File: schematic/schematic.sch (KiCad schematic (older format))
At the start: 1 part

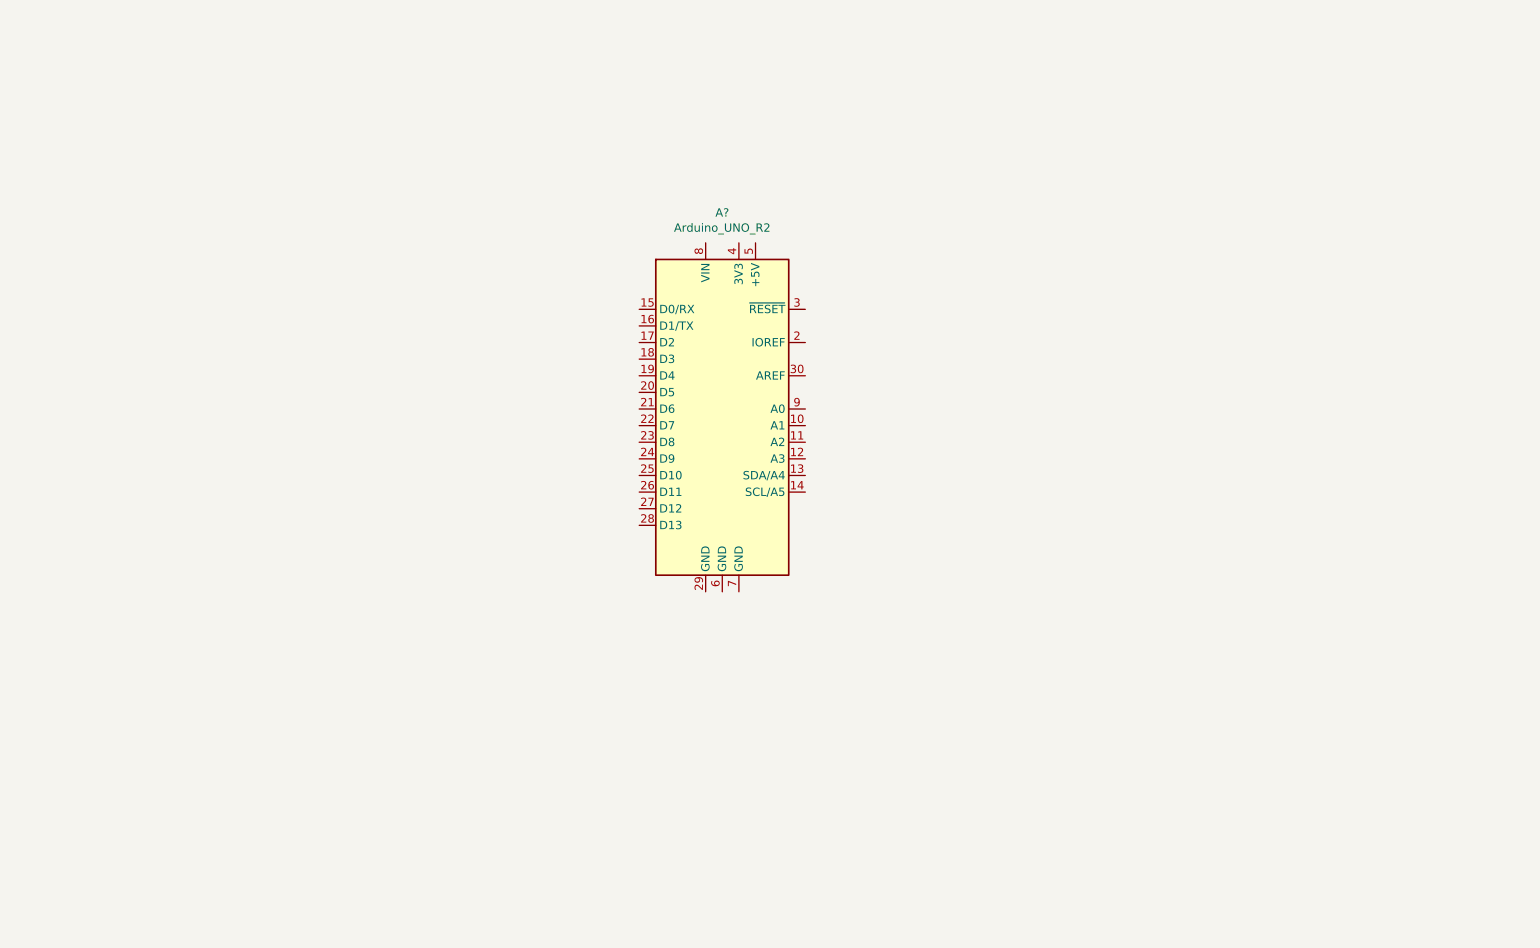
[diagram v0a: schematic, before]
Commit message: Finish pressure sensor symbol, start wiring
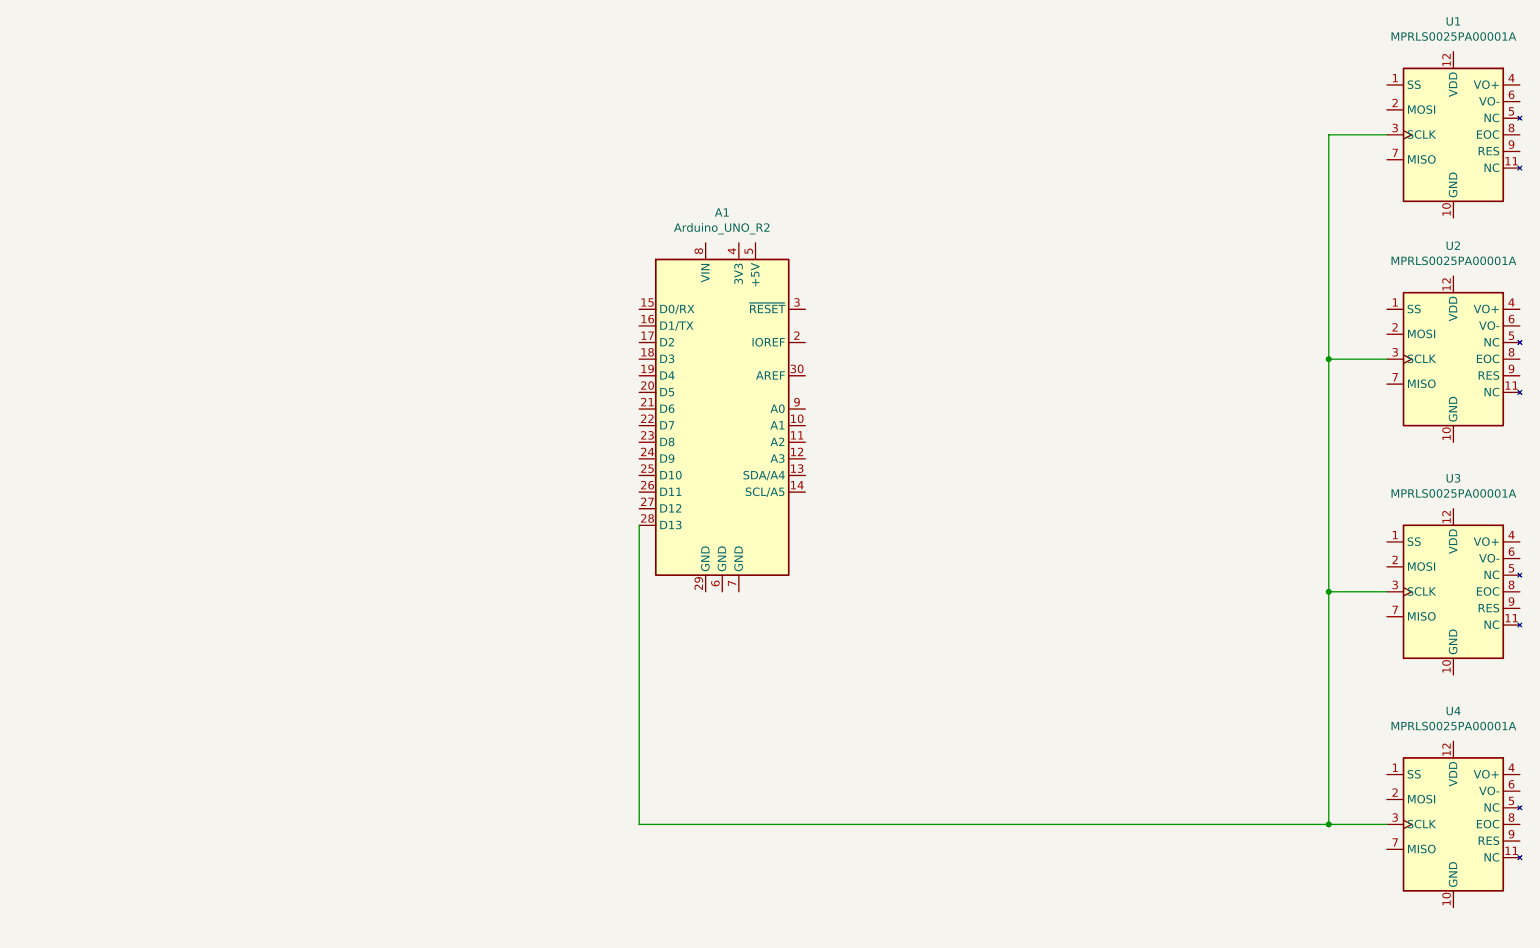
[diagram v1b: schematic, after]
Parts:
- added U1, U2, U3, U4: MPRLS0025PA00001A, symbol ventilator:MPRLS0025PA00001A
- gave numbers to parts that had none: 1
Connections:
- net at A1.28 (D13): now also U1.3 (SCLK), U2.3 (SCLK), U3.3 (SCLK), U4.3 (SCLK)
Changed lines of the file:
@@
 encoding utf-8
 Sheet 1 1
-Title ""
+Title "Ventilator"
 Date ""
-Rev ""
+Rev "1A"
 Comp ""
 Comment1 ""
@@
 $EndDescr
 $Comp
-L MCU_Module:Arduino_UNO_R2 A?
+L MCU_Module:Arduino_UNO_R2 A1
 U 1 1 5E80F89B
 P 5900 3050
-F 0 "A?" H 5900 4231 50  0000 C CNN
+F 0 "A1" H 5900 4231 50  0000 C CNN
 F 1 "Arduino_UNO_R2" H 5900 4140 50  0000 C CNN
 F 2 "Module:Arduino_UNO_R2" H 5900 3050 50  0001 C CIN
@@
 	1    0    0    -1
 $EndComp
+$Comp
+L ventilator:MPRLS0025PA00001A U1
+U 1 1 5E810603
+P 10300 1400
+F 0 "U1" H 10300 2081 50  0000 C CNN
+F 1 "MPRLS0025PA00001A" H 10300 1990 50  0000 C CNN
+F 2 "" H 11300 950 50  0001 C CNN
+F 3 "https://sensing.honeywell.com/index.php?ci_id=172626" H 11450 1450 50  0001 C CNN
+	1    10300 1400
+	1    0    0    -1
+$EndComp
+$Comp
+L ventilator:MPRLS0025PA00001A U2
+U 1 1 5E8111B8
+P 10300 2750
+F 0 "U2" H 10300 3431 50  0000 C CNN
+F 1 "MPRLS0025PA00001A" H 10300 3340 50  0000 C CNN
+F 2 "" H 11300 2300 50  0001 C CNN
+F 3 "https://sensing.honeywell.com/index.php?ci_id=172626" H 11450 2800 50  0001 C CNN
+	1    10300 2750
+	1    0    0    -1
+$EndComp
+$Comp
+L ventilator:MPRLS0025PA00001A U3
+U 1 1 5E811D8D
+P 10300 4150
+F 0 "U3" H 10300 4831 50  0000 C CNN
+F 1 "MPRLS0025PA00001A" H 10300 4740 50  0000 C CNN
+F 2 "" H 11300 3700 50  0001 C CNN
+F 3 "https://sensing.honeywell.com/index.php?ci_id=172626" H 11450 4200 50  0001 C CNN
+	1    10300 4150
+	1    0    0    -1
+$EndComp
+$Comp
+L ventilator:MPRLS0025PA00001A U4
+U 1 1 5E8127FE
+P 10300 5550
+F 0 "U4" H 10300 6231 50  0000 C CNN
+F 1 "MPRLS0025PA00001A" H 10300 6140 50  0000 C CNN
+F 2 "" H 11300 5100 50  0001 C CNN
+F 3 "https://sensing.honeywell.com/index.php?ci_id=172626" H 11450 5600 50  0001 C CNN
+	1    10300 5550
+	1    0    0    -1
+$EndComp
+Wire Wire Line
+	5400 5550 9550 5550
+Wire Wire Line
+	5400 3750 5400 5550
+Wire Wire Line
+	9900 4150 9550 4150
+Wire Wire Line
+	9550 4150 9550 5550
+Connection ~ 9550 5550
+Wire Wire Line
+	9550 5550 9900 5550
+Wire Wire Line
+	9900 2750 9550 2750
+Wire Wire Line
+	9550 2750 9550 4150
+Connection ~ 9550 4150
+Wire Wire Line
+	9550 2750 9550 1400
+Wire Wire Line
+	9550 1400 9900 1400
+Connection ~ 9550 2750
 $EndSCHEMATC

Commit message: finished electrical schematic
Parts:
- added Diode (x2): 1N4001, Diode_THT:D_DO-41_SOD81_P10.16mm_Horizontal, symbol Diode:1N4001
- added MOSFET (x2): BSB280N15NZ3, Package_DirectFET:DirectFET_MZ, symbol Transistor_FET:BSB280N15NZ3
- added Resistor (x2): 10 kohm, symbol Device:R
- added Solenoid (x2): Valve, symbol ventilator:Valve
- A1: symbol MCU_Module:Arduino_UNO_R2 -> schematic-rescue:Arduino_UNO_R2-MCU_Module
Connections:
- net labels added: +12V
- wire segments 9 -> 68
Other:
- moved on the sheet: U1, U2, U3, U4
